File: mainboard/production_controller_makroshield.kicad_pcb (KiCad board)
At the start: 2 copper layers, 145.4 x 193.7 mm, 95 parts, among them J1 CON_TERM_BLK_1X2_TB008A-508-0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, J10 CON_CONNAXIO_MOTOR_DRIVER, J11 CON_CONNAXIO_MOTOR_DRIVER, J12 CON_CONNAXIO_MOTOR_DRIVER, J13 CON_CONNAXIO_MOTOR_DRIVER, J14 CON_CONNAXIO_MOTOR_DRIVER, J15 CON_CONNAXIO_MOTOR_DRIVER, J16 CON_CONNAXIO_MOTOR_DRIVER, J17 CON_CONNAXIO_MOTOR_DRIVER, J18 CON_CONNAXIO_MOTOR_DRIVER, J19 CON_CONNAXIO_MOTOR_DRIVER, J2 CON_HDR_MIKROBUS_ADDON_TH, J20 CON_CONNAXIO_MOTOR_DRIVER, J3 CON_BARREL_2.1X5.5_PJ-002A, J4 CON_HDR_MIKROBUS_SOCKET_TH, J5 CON_CONNAXIO_MOTOR_DRIVER, J6 CON_CONNAXIO_MOTOR_DRIVER, J7 CON_CONNAXIO_MOTOR_DRIVER, J8 CON_CONNAXIO_MOTOR_DRIVER, J9 CON_CONNAXIO_MOTOR_DRIVER, Q1 TRX_PMOS_AOD4189, Q2 TRX_NPN_MMBT3904-TP, U1 IO_EXP_PI4IOE5V6416ZDEX, U2 IO_EXP_PI4IOE5V6416ZDEX, U3 SUN_CUR_ACS711KEXLT-31AB-T, U4 ADC_NAU7802SGI

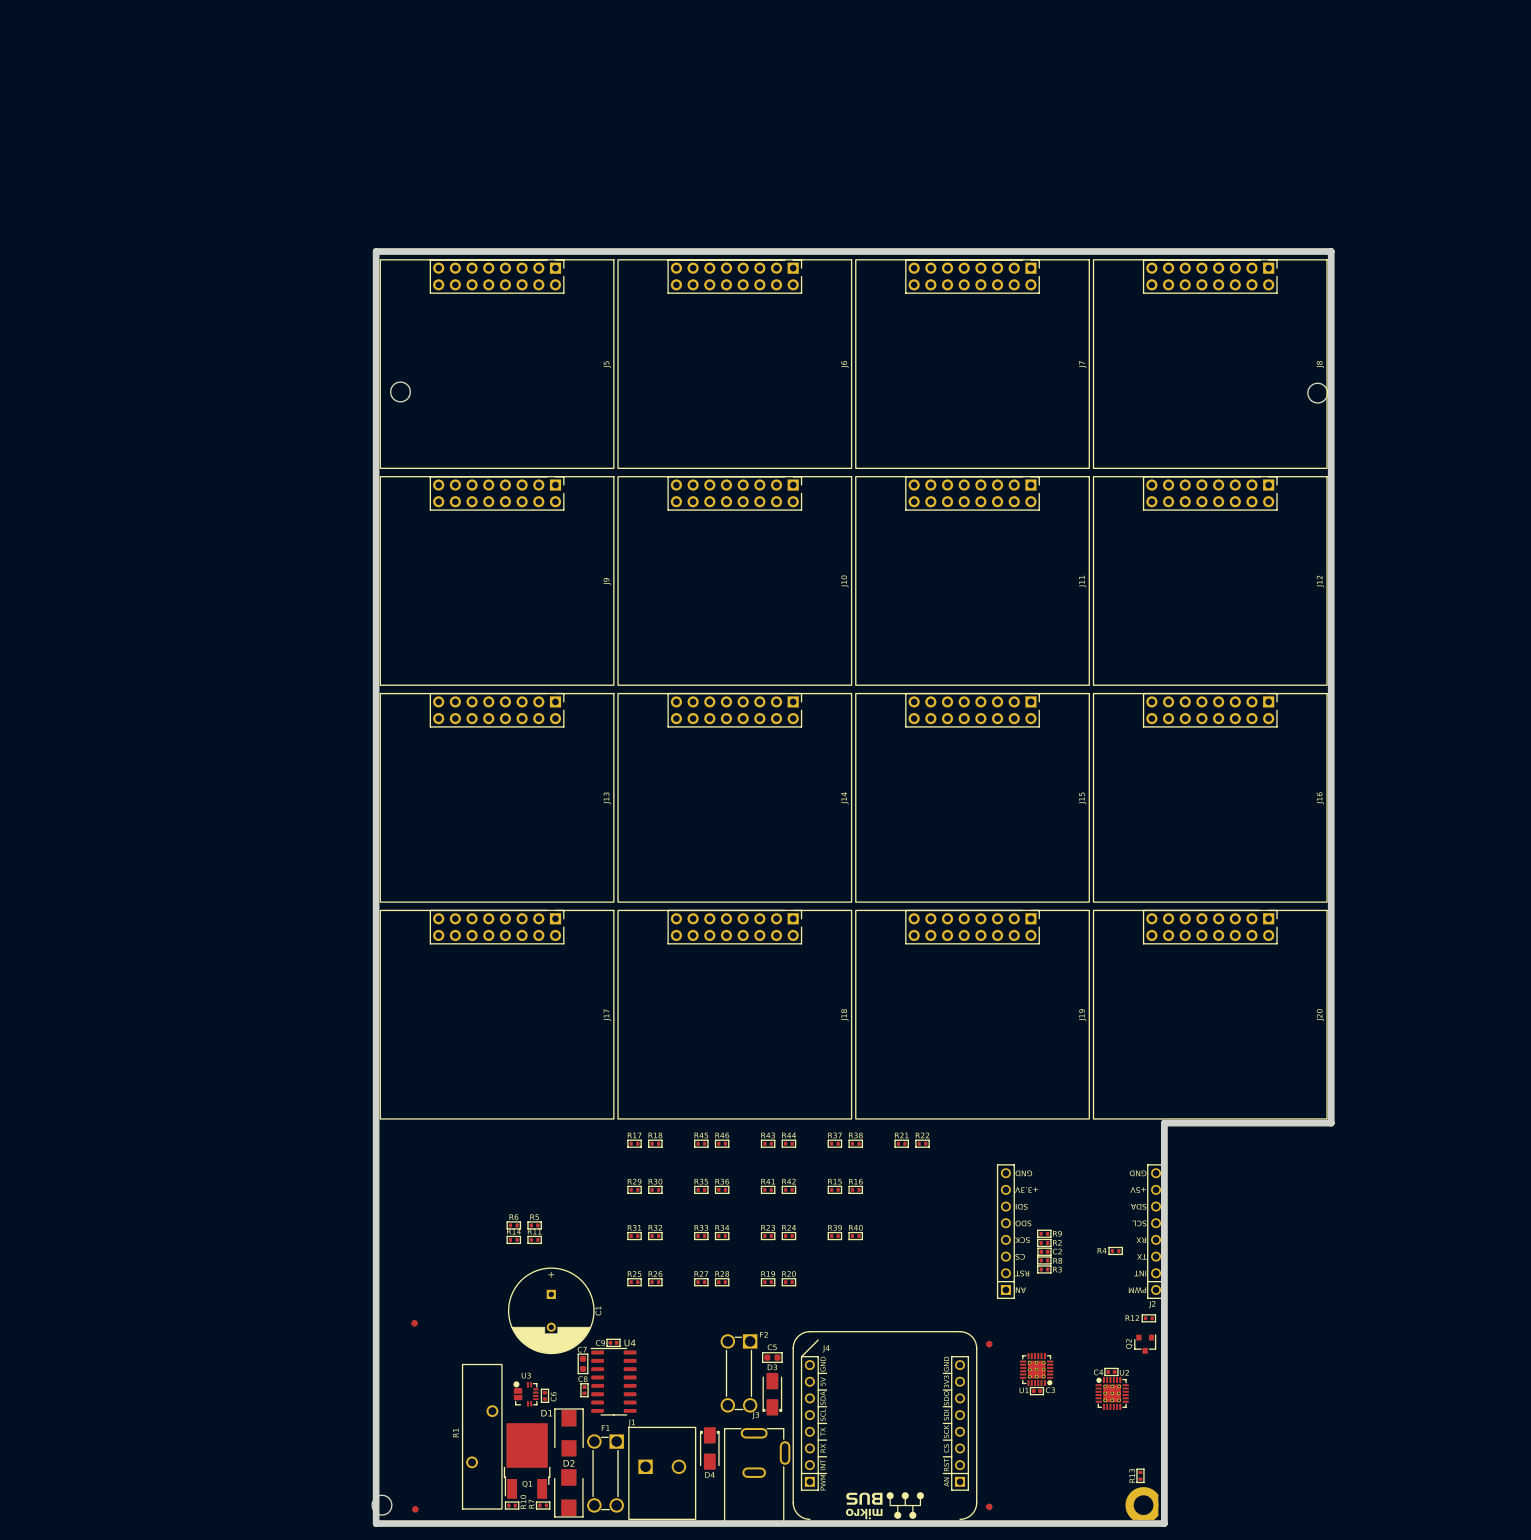
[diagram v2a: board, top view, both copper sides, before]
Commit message: Position drive rmodules, choose enclosure, shape PCB
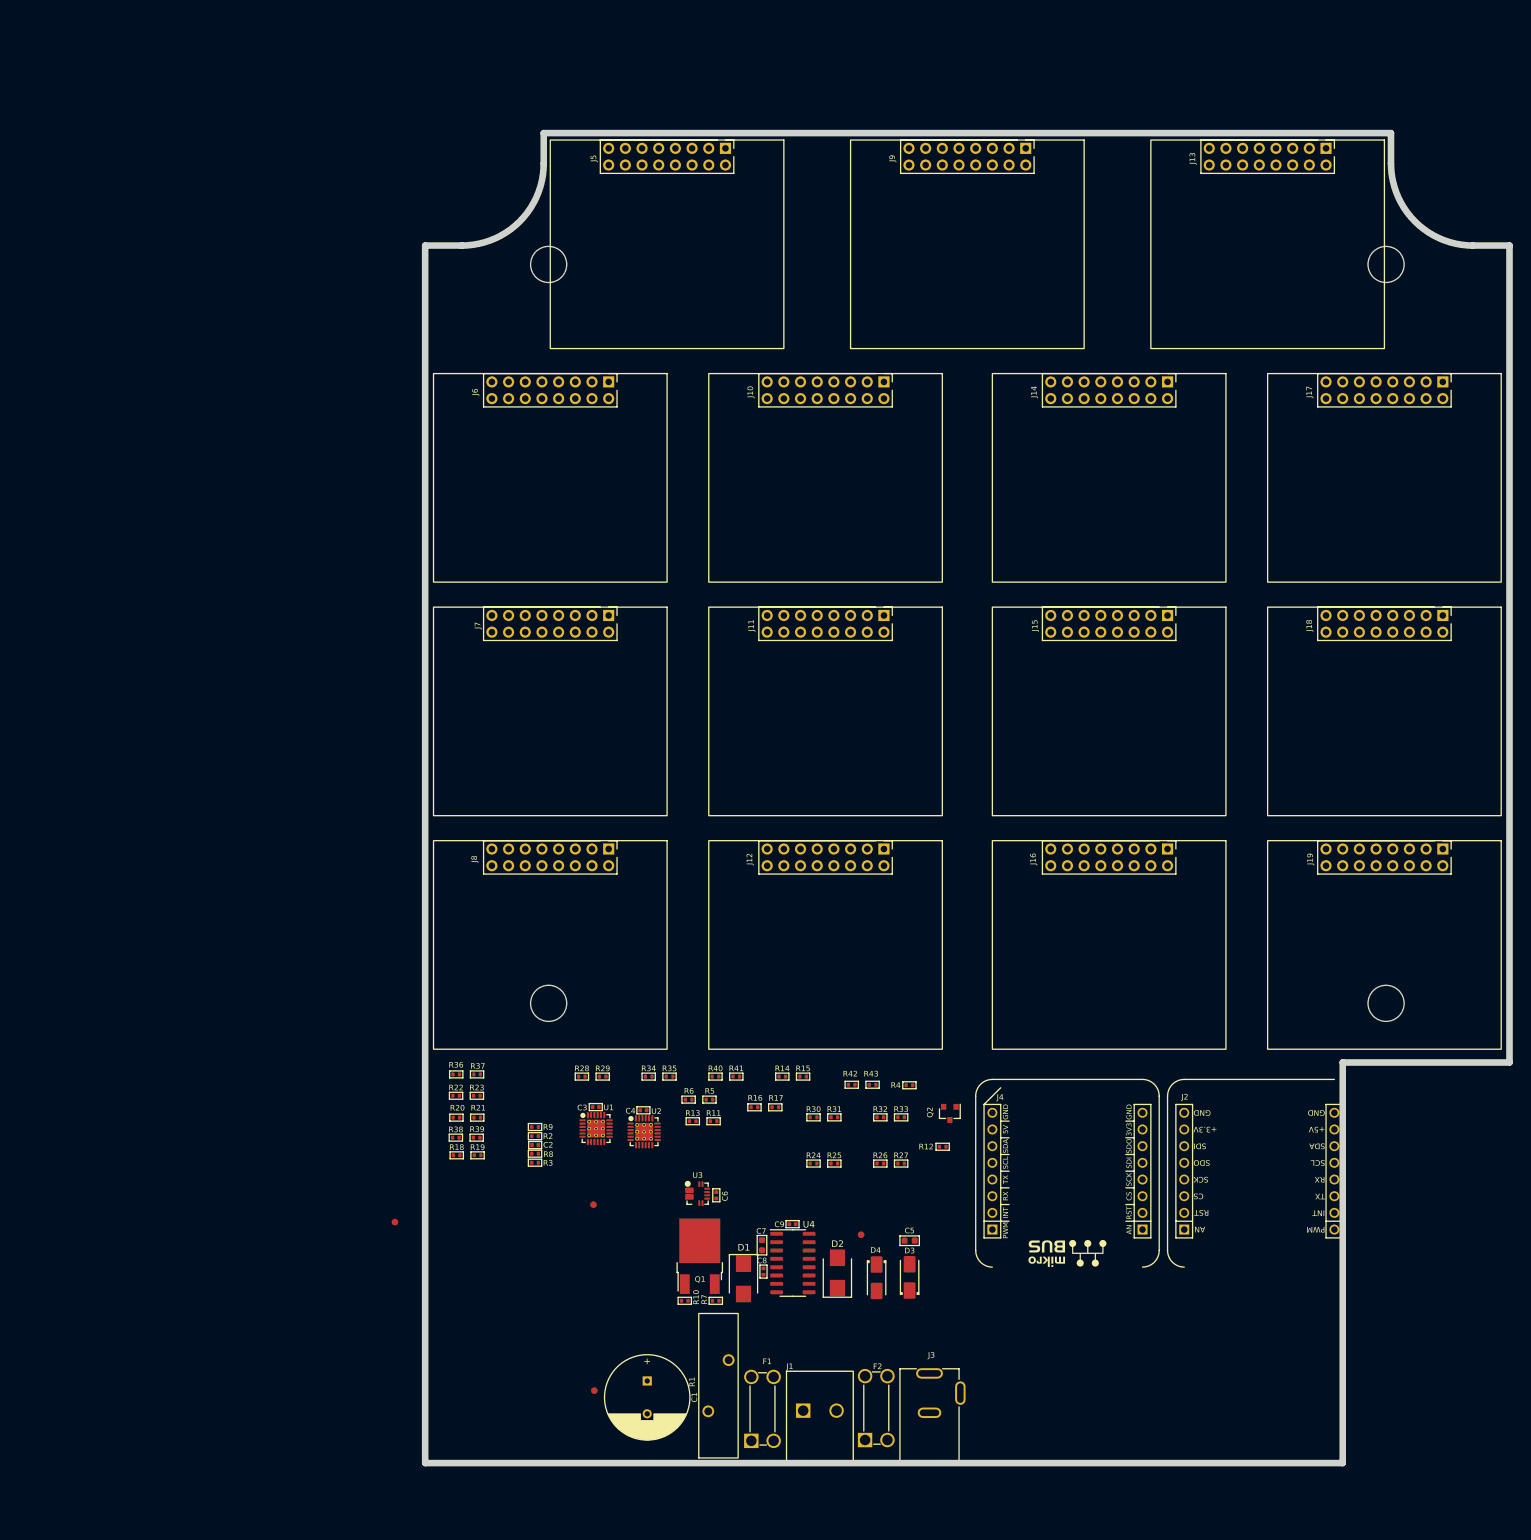
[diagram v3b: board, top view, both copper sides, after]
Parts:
- removed J20: CON_CONNAXIO_MOTOR_DRIVER, connaxio-connectors:CON_CONNAXIO_MOTOR_DRIVER
- removed the R13 at (186.5, 239.1)
- removed R45, R46: RES_12.4KΩ_1%_0402, connaxio-resistors:RES_0402_1005M
- MTH1: value MTH_M2.5_PTH_CORNER -> MTH_M5_NPTH; footprint connaxio-mechanical:MTH_M2.5_PTH_CORNER -> connaxio-mechanical:MTH_M5_NPTH
- MTH2, MTH3, MTH4: value MTH_M2.5_NPTH -> MTH_M5_NPTH; footprint connaxio-mechanical:MTH_M2.5_NPTH -> connaxio-mechanical:MTH_M5_NPTH
- moved MTH1 192.5 mm to (223.9, 54.7), turned to 0 degrees
- moved MTH4 190.6 mm to (96.4, 54.7)
- moved MTH3 176.6 mm to (223.9, 167.2)
- moved J17 157.9 mm to (223.6, 87.2)
- moved MTH2 149.5 mm to (96.4, 167.2)
- moved J13 144.5 mm to (205.8, 51.6)
- moved J8 133.9 mm to (96.6, 158.3)
- moved J18 109.2 mm to (223.6, 122.7)
- moved F4 92.4 mm to (73.0, 200.5)
- moved J9 88.1 mm to (160.1, 51.6)
- moved J7 83.2 mm to (96.6, 122.7)
- moved C4 81.6 mm to (110.8, 183.5)
- moved U2 81.6 mm to (110.9, 186.7)
- moved J12 80.6 mm to (138.5, 158.3)
- moved C3 79.9 mm to (103.5, 183.0), turned to 180 degrees
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- renumbered R14 to R13, R15 to R14, R16 to R15, R17 to R16, R18 to R17, R19 to R18, R20 to R19, R21 to R20, R22 to R21, R23 to R22, R24 to R23, R25 to R24, R26 to R25, R27 to R26, R28 to R27, R29 to R28, R30 to R29, R31 to R30, R32 to R31, R33 to R32, R34 to R33, R35 to R34, R36 to R35, R37 to R36, R38 to R37, R39 to R38, R40 to R39, R41 to R40, R42 to R41, R43 to R42, R44 to R43
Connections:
- U2 pad 16: CTRLA16 -> unconnected-(U2-Pad16)
- U2 pad 17: CTRLB16 -> unconnected-(U2-Pad17)
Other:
- board size 145.4 x 193.7 mm -> 165.1 x 202.5 mm
- board text added: "NBF-32x16 enclosure: M5 X 10 mm Hole spacing: 127.5 x 112.5 mm"

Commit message: Routing mainboard
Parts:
- removed the J3 at (154.4, 230.0)
- added F2: FUS_BLADE_MINI_3588-1, connaxio-connectors:FUS_BLADE_MINI_3588-1, F.Cu at (101.4, 229.4)
- added J2: CON_TERM_BLK_1X2_TB008A-508-02BE, connaxio-connectors:CON_TERM_BLK_1X2_TB008A-508-02BE, F.Cu at (115.7, 228.8)
- added J4: CON_TERM_BLK_1X2_TB008A-508-02BE, connaxio-connectors:CON_TERM_BLK_1X2_TB008A-508-02BE, F.Cu at (153.8, 228.8)
- moved R3 105.9 mm to (199.7, 201.6), turned to 180 degrees
- moved R8 105.9 mm to (199.7, 200.2)
- moved R2 105.9 mm to (199.7, 197.4)
- moved R9 105.9 mm to (199.7, 196.0)
- moved C2 105.9 mm to (199.7, 198.8)
- moved F5 97.0 mm to (168.0, 180.8)
- moved R6 92.9 mm to (210.3, 188.9)
- moved R5 89.9 mm to (210.3, 191.4)
- moved R38 77.5 mm to (159.4, 180.0), turned to 90 degrees
- moved R39 73.0 mm to (158.0, 180.0), turned to 90 degrees
- moved R4 62.1 mm to (210.3, 199.1)
- moved F6 61.4 mm to (162.7, 210.4)
- moved R36 60.3 mm to (142.6, 180.0), turned to 90 degrees
- moved R22 57.6 mm to (139.8, 180.0), turned to 90 degrees
- moved R37 55.8 mm to (141.2, 180.0), turned to 90 degrees
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- renumbered F2 to F3, F3 to F4, F4 to F5, F5 to F6, F6 to F7, J9 to J10, J10 to J11, J11 to J12, J12 to J13, J13 to J14, J14 to J15, J15 to J16, J16 to J17, J17 to J18, J18 to J19, J19 to J20, J2 to J3, J4 to J5, J5 to J6, J6 to J7, J7 to J8, J8 to J9
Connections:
- D1 pad 1: /24V_CS -> +24VDC
- D1 pad 2: /24V_Neg -> GND
- D2 pad 2: /24V_Neg -> GND
- D3 pad 1: Net-(D3-Pad1) -> +5V
- D3 pad 2: +5V -> Net-(D3-Pad2)
- D4 pad 1: Net-(D3-Pad1) -> Net-(D3-Pad2)
- F3 pad 3: Net-(D3-Pad1) -> Net-(D3-Pad2)
- F3 pad 4: Net-(D3-Pad1) -> Net-(D3-Pad2)
- J1 pad 2: /24V_Neg -> GND
- Q1 pad 3: /24V_CS -> /CS+
- R1 pad 2: /24V_CS -> /CS+
- U3 pad 1: /24V_CS -> +24VDC
- U3 pad 2: /24V_CS -> +24VDC
- U3 pad 3: +24VDC -> /CS+
- U3 pad 4: +24VDC -> /CS+
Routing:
- net RST_MOT: track 0.00 -> 470.5 mm
- net FAULT: track 0.00 -> 467.2 mm
- net CTRLA13: track 0.00 -> 205.5 mm
- net CTRLB13: track 0.00 -> 204.1 mm
- net CTRLB9: track 0.00 -> 193.1 mm
- net CTRLA9: track 0.00 -> 192.5 mm
- net CTRLA5: track 0.00 -> 172.0 mm
- net CTRLB5: track 0.00 -> 169.1 mm
- net CTRLA14: track 0.00 -> 165.0 mm
- net CTRLB14: track 0.00 -> 164.0 mm
- net CTRLA1: track 0.00 -> 160.5 mm
- net CTRLB1: track 0.00 -> 159.9 mm
- net CTRLB10: track 0.00 -> 156.5 mm
- net CTRLA10: track 0.00 -> 153.8 mm
- net CTRLB15: track 0.00 -> 127.6 mm
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- added copper zone on F.Cu, net +24VDC
- added copper zone on B.Cu, net /CS+
- added copper zone on F.Cu, net /CS+
- added copper zone on B.Cu, net GND
- added copper zone on F.Cu, net GND
- added copper zone on B.Cu, net Net-(D2-Pad1)
- added copper zone on F.Cu, net Net-(D2-Pad1)
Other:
- board text added: "1"
- board text added: "10"
- board text added: "11"
- board text added: "12"
- board text added: "13"
- board text added: "14"
- board text added: "15"
- board text added: "2"
- board text added: "24V IN + -"
- board text added: "24V OUT + -"
- board text added: "3"
- board text added: "4"
- board text added: "5"
- board text added: "5V IN + -"
- board text added: "6"
- board text added: "7"
- board text added: "8"
- board text added: "9"
- board text added: "Warning: the 24V power supply must be grounded (3-prong wall plug), while the 5V power supply must be floating (2-prong wall plug). Avertissement: l'alimentation 24V doit être mise à la terre (connecteur mural 3 prises) et l'alimentation 5V doit être flottante (connecteur mural 2 prises)."

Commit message: Routing
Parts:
- moved F2 26.6 mm to (115.0, 206.6)
- moved C5 4.12 mm to (159.2, 194.7), turned to -90 degrees
- moved U4 0.65 mm to (150.0, 198.7)
- moved C7 0.65 mm to (145.3, 196.0)
- moved C8 0.65 mm to (145.5, 200.0)
- moved C9 0.65 mm to (149.9, 192.8)
- moved D3 0.38 mm to (156.6, 195.9)
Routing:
- net +3.3V: track 29.3 -> 791.8 mm, vias 32 -> 33
- net FAULT: track 467.2 -> 727.9 mm, vias 0 -> 2
- net RST_MOT: track 470.5 -> 691.9 mm, vias 0 -> 2
- net /NTC_BYPASS: track 1.41 -> 95.2 mm
- net /RST_IO: track 0.00 -> 78.3 mm, vias 0 -> 2
- net /DRDY: track 0.00 -> 74.7 mm
- net GND: track 4.50 -> 27.2 mm, vias 101 -> 164
- net Net-(Q1-Pad1): track 0.00 -> 6.47 mm
- net CTRLB12: track 91.4 -> 94.6 mm
- net CTRLB8: track 47.5 -> 50.0 mm
- net CTRLB4: track 59.6 -> 57.2 mm
- net Net-(Q2-Pad3): track 0.00 -> 2.08 mm
- net CTRLA8: track 48.8 -> 50.1 mm
- net CTRLA12: track 89.2 -> 90.6 mm
- net CTRLA13: track 205.5 -> 204.4 mm
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- added copper zone on B.Cu, net Net-(D3-Pad2)
- added copper zone on F.Cu, net Net-(D3-Pad2)
- added copper zone on B.Cu, net Net-(F1-Pad1)
- added copper zone on F.Cu, net Net-(F1-Pad1)

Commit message: DRC pass
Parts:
- moved C4 5.50 mm to (152.2, 188.4), turned to 0 degrees
- moved C3 5.49 mm to (129.8, 188.4), turned to 0 degrees
- moved R4 4.95 mm to (210.3, 194.1)
- moved F5 3.87 mm to (170.5, 183.7)
- moved D3 2.62 mm to (157.8, 198.2), turned to 180 degrees
- moved U1 2.03 mm to (129.0, 184.6), turned to 180 degrees
- moved U2 1.91 mm to (151.5, 184.6), turned to 180 degrees
- moved C5 0.77 mm to (159.1, 195.5), turned to 180 degrees
- turned R2 to 180 degrees
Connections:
- U1 pad 1: CTRLA1 -> CTRLA5
- U1 pad 10: CTRLA5 -> CTRLA1
- U1 pad 11: CTRLB5 -> CTRLB1
- U1 pad 12: CTRLA6 -> CTRLA2
- U1 pad 13: CTRLB6 -> CTRLB2
- U1 pad 14: CTRLA7 -> CTRLA3
- U1 pad 15: CTRLB7 -> CTRLB3
- U1 pad 16: CTRLA8 -> CTRLA4
- U1 pad 17: CTRLB8 -> CTRLB4
- U1 pad 2: CTRLB1 -> CTRLB5
- U1 pad 3: CTRLA2 -> CTRLA6
- U1 pad 4: CTRLB2 -> CTRLB6
- U1 pad 5: CTRLA3 -> CTRLA7
- U1 pad 6: CTRLB3 -> CTRLB7
- U1 pad 7: CTRLA4 -> CTRLA8
- U1 pad 8: CTRLB4 -> CTRLB8
- U2 pad 1: CTRLA9 -> unconnected-(U2-Pad1)
- U2 pad 10: CTRLA13 -> CTRLA9
- U2 pad 11: CTRLB13 -> CTRLB9
- U2 pad 12: CTRLA14 -> CTRLA10
- U2 pad 13: CTRLB14 -> CTRLB10
- U2 pad 14: CTRLA15 -> CTRLA11
- U2 pad 15: CTRLB15 -> CTRLB11
- U2 pad 16: unconnected-(U2-Pad16) -> CTRLA12
- U2 pad 17: unconnected-(U2-Pad17) -> CTRLB12
- U2 pad 2: CTRLB9 -> unconnected-(U2-Pad2)
- U2 pad 3: CTRLA10 -> CTRLA13
- U2 pad 4: CTRLB10 -> CTRLB13
- U2 pad 5: CTRLA11 -> CTRLA14
- U2 pad 6: CTRLB11 -> CTRLB14
- U2 pad 7: CTRLA12 -> CTRLA15
- U2 pad 8: CTRLB12 -> CTRLB15
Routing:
- net /I2C_SCL: track 0.00 -> 111.6 mm, vias 0 -> 2
- net /I2C_SDA: track 0.00 -> 107.2 mm
- net +3.3V: track 791.8 -> 898.3 mm, vias 33 -> 49
- net /INT_IO: track 0.00 -> 104.7 mm, vias 0 -> 11
- net RST_MOT: track 691.9 -> 787.6 mm, vias 2 -> 15
- net FAULT: track 727.9 -> 800.5 mm, vias 2 -> 12
- net +5V: track 0.00 -> 68.2 mm, vias 0 -> 2
- net /RST_IO: track 78.3 -> 95.4 mm, vias 2 -> 8
- net /DRDY: track 74.7 -> 84.2 mm, vias 0 -> 1
- net CTRLA13: track 204.4 -> 196.6 mm
- net CTRLB12: track 94.6 -> 87.6 mm
- net CTRLB13: track 204.0 -> 197.1 mm
- net CTRLA14: track 165.4 -> 158.5 mm
- net CTRLA5: track 171.1 -> 164.5 mm
- net Net-(J3-Pad2): track 0.00 -> 6.57 mm
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- added copper zone on B.Cu, net Net-(F2-Pad3)
- added copper zone on F.Cu, net Net-(F2-Pad3)
- added copper zone on B.Cu, net Net-(F3-Pad1)
- added copper zone on F.Cu, net Net-(F3-Pad1)

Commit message: Add high-current pathways and extra capacitors. DRC pass
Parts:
- added C3: CAP_AE_1MF_50V_TH_12.5MM, connaxio-capacitors:CAPAE_RAD_D12.5_H26.5_P5, F.Cu at (104.2, 190.0)
- added C4: CAP_AE_1MF_50V_TH_12.5MM, connaxio-capacitors:CAPAE_RAD_D12.5_H26.5_P5, F.Cu at (89.0, 190.0)
- added C5: CAP_AE_1MF_50V_TH_12.5MM, connaxio-capacitors:CAPAE_RAD_D12.5_H26.5_P5, F.Cu at (89.0, 205.3)
- moved C1 0.13 mm to (104.2, 205.3)
- renumbered C7 to C10, C8 to C11, C9 to C12, C3 to C6, C4 to C7, C5 to C8, C6 to C9
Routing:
- net +24VDC: vias 0 -> 97
- added copper zone on B.Cu, net +24VDC
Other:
- board text added: "Warning: the 24V power supply must be grounded (3-prong wall plug), while the optional 5V power supply must be floating (2-prong wall plug). Avertissement: l'alimentation 24V doit être mise à la terre (connecteur mural 3 prises) et l'alimentation optionnelle 5V doit être flottante (connecteur mural 2 prises)."
- board text removed: "Warning: the 24V power supply must be grounded (3-prong wall plug), while the 5V power supply must be floating (2-prong wall plug). Avertissement: l'alimentation 24V doit être mise à la terre (connecteur mural 3 prises) et l'alimentation 5V doit être flottante (connecteur mural 2 prises)."
